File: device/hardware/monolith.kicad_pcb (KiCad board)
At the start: 2 copper layers, 116 parts, among them J1 CAN, J10 Conn_01x02_Pin, J11 UART, J12 DIN1/2, J13 DIN3/4, J14 Micro_SD_Card, J2 GPS, J3 I2C, J4 AIN1/2, J5 AIN3/4, J6 AIN5/6, J7 Conn_01x02_Pin, J8 Conn_01x02_Pin, J9 Conn_01x02_Pin, U1 ESP32-S3-WROOM-1-N4, U10 LMV321, U11 AMS1117-3.3, U2 MCP6002-xSN, U3 SN65HVD230, U4 TPS5430DDA, U5 MCP6002-xSN, U6 MPU-6050, U7 MCP6002-xSN, U8 AMS1117-3.3, U9 PCF8563T, Y1 FC135

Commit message: update: PCB prototype
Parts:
- removed C19: 47uF, Capacitor_SMD:C_1206_3216Metric
- removed RV1, RV2, RV3, RV4: 1k, Potentiometer_THT:Potentiometer_Bourns_3266W_Vertical
- removed TP3, TP4, TP5, TP6: TestPoint, Connector_PinHeader_2.54mm:PinHeader_1x01_P2.54mm_Vertical
- added C29: 0.1uF, Capacitor_SMD:C_0603_1608Metric, F.Cu at (97.9, 118.6)
- added C30: 22uF, Capacitor_SMD:C_0603_1608Metric, F.Cu at (147.8, 112.6)
- added C31: 22nF, Capacitor_SMD:C_0603_1608Metric, F.Cu at (125.5, 116.7)
- added C32: 22nF, Capacitor_SMD:C_0603_1608Metric, F.Cu at (128.9, 116.7)
- added C33: 22nF, Capacitor_SMD:C_0603_1608Metric, F.Cu at (136.6, 116.7)
- added C34: 22nF, Capacitor_SMD:C_0603_1608Metric, F.Cu at (140.0, 116.7)
- added C35: 22nF, Capacitor_SMD:C_0603_1608Metric, F.Cu at (147.8, 119.9)
- added C36: 22nF, Capacitor_SMD:C_0603_1608Metric, F.Cu at (151.0, 119.9)
- added C37: 22nF, Capacitor_SMD:C_0603_1608Metric, F.Cu at (155.5, 119.2)
- added C38: 0.1uF, Capacitor_SMD:C_0603_1608Metric, F.Cu at (70.4, 114.9)
- added JP6: Jumper_2_Small_Open, Connector_PinHeader_2.54mm:PinHeader_1x02_P2.54mm_Vertical, F.Cu at (136.2, 134.4)
- added JP7: Jumper_2_Small_Open, Connector_PinHeader_2.54mm:PinHeader_1x02_P2.54mm_Vertical, F.Cu at (140.4, 134.4)
- added JP8: TERMINAL, Connector_PinHeader_2.54mm:PinHeader_1x02_P2.54mm_Vertical, F.Cu at (72.2, 130.1)
- added JP9: Jumper_2_Small_Bridged, Jumper:SolderJumper-2_P1.3mm_Bridged_RoundedPad1.0x1.5mm, F.Cu at (147.7, 107.1)
- added R32: 220, Resistor_SMD:R_0603_1608Metric, F.Cu at (114.0, 138.4)
- added R33: 4.7k, Resistor_SMD:R_0603_1608Metric, F.Cu at (106.3, 116.6)
- added R34: 100, Resistor_SMD:R_0603_1608Metric, F.Cu at (157.9, 120.0)
- added R35: 220, Resistor_SMD:R_0603_1608Metric, F.Cu at (107.1, 138.4)
- added R36: 220, Resistor_SMD:R_0603_1608Metric, F.Cu at (102.9, 138.4)
- added R37: 4.7k, Resistor_SMD:R_0603_1608Metric, F.Cu at (108.0, 115.8)
- added R38: 4.7k, Resistor_SMD:R_0603_1608Metric, F.Cu at (118.2, 115.0)
- added R39: 4.7k, Resistor_SMD:R_0603_1608Metric, F.Cu at (119.9, 115.8)
- added REF**: MountingHole_3mm_Pad_TopBottom, MountingHole:MountingHole_3mm_Pad_TopBottom, F.Cu at (68.3, 88.2)
- added REF**: MountingHole_3mm_Pad_TopBottom, MountingHole:MountingHole_3mm_Pad_TopBottom, F.Cu at (156.3, 136.8)
- added REF**: MountingHole_3mm_Pad_TopBottom, MountingHole:MountingHole_3mm_Pad_TopBottom, F.Cu at (68.3, 136.8)
- added REF**: MountingHole_3mm_Pad_TopBottom, MountingHole:MountingHole_3mm_Pad_TopBottom, F.Cu at (138.8, 88.2)
- added U12: AMS1117-3.3, Package_TO_SOT_SMD:SOT-223-3_TabPin2, F.Cu at (142.4, 109.6)
- added U13: ADS1115IDGS, Package_SO:TSSOP-10_3x3mm_P0.5mm, F.Cu at (150.4, 115.8)
- C13, C14: value 47uF -> 22nF; footprint Capacitor_SMD:C_1206_3216Metric -> Capacitor_SMD:C_0603_1608Metric
- C16: value 0.1uF -> 47uF; footprint Capacitor_SMD:C_0603_1608Metric -> Capacitor_SMD:C_1206_3216Metric
- C17: value 22nF -> 47uF; footprint Capacitor_SMD:C_0603_1608Metric -> Capacitor_SMD:C_1206_3216Metric
- C18: value 22nF -> 0.1uF
- C22, C28: value 22uF -> 0.1uF
- C23: value 20pF -> 22uF
- C25: value 22nF -> 20pF
- C26: value 10uF -> 22nF
- C27: value 0.1uF -> 10uF
- J1, J2, J3, J4, J5, J6: footprint Connector_Molex:Molex_Mini-Fit_Jr_5566-04A2_2x02_P4.20mm_Vertical -> Connector_Molex:Molex_Mini-Fit_Jr_5569-04A2_2x02_P4.20mm_Horizontal
- J10: value Conn_01x02_Pin -> UART; footprint Connector_PinHeader_2.54mm:PinHeader_1x02_P2.54mm_Vertical -> Connector_PinHeader_2.54mm:PinHeader_1x04_P2.54mm_Vertical
- J11: value UART -> DIN1/2; footprint Connector_PinHeader_2.54mm:PinHeader_1x04_P2.54mm_Vertical -> Connector_Molex:Molex_Mini-Fit_Jr_5569-04A2_2x02_P4.20mm_Horizontal
- J12: value DIN1/2 -> DIN3/4; footprint Connector_Molex:Molex_Mini-Fit_Jr_5566-04A2_2x02_P4.20mm_Vertical -> Connector_Molex:Molex_Mini-Fit_Jr_5569-04A2_2x02_P4.20mm_Horizontal
- J13: value DIN3/4 -> Micro_SD_Card; footprint Connector_Molex:Molex_Mini-Fit_Jr_5566-04A2_2x02_P4.20mm_Vertical -> parts:TF115BCP9
- J14: value Micro_SD_Card -> I2C2; footprint parts:TF115BCP9 -> Connector_PinHeader_1.00mm:PinHeader_1x02_P1.00mm_Vertical
- J7: value Conn_01x02_Pin -> USB; footprint Connector_PinHeader_2.54mm:PinHeader_1x02_P2.54mm_Vertical -> Connector_PinHeader_1.00mm:PinHeader_1x02_P1.00mm_Vertical
- J8: value Conn_01x02_Pin -> CAN; footprint Connector_PinHeader_2.54mm:PinHeader_1x02_P2.54mm_Vertical -> Connector_PinHeader_1.00mm:PinHeader_1x02_P1.00mm_Vertical
- J9: value Conn_01x02_Pin -> I2C1; footprint Connector_PinHeader_2.54mm:PinHeader_1x02_P2.54mm_Vertical -> Connector_PinHeader_1.00mm:PinHeader_1x02_P1.00mm_Vertical
- JP1: value Jumper_2_Small_Open -> RESET; footprint Connector_PinHeader_2.54mm:PinHeader_1x02_P2.54mm_Vertical -> Connector_PinHeader_1.00mm:PinHeader_1x02_P1.00mm_Vertical
- JP4: value Jumper_2_Small_Open -> BOOT; footprint Connector_PinHeader_2.54mm:PinHeader_1x02_P2.54mm_Vertical -> Connector_PinHeader_1.00mm:PinHeader_1x02_P1.00mm_Vertical
- JP5: value Jumper_2_Small_Bridged -> BTN; footprint Jumper:SolderJumper-2_P1.3mm_Bridged_RoundedPad1.0x1.5mm -> Connector_PinHeader_1.00mm:PinHeader_1x02_P1.00mm_Vertical
- R10, R11, R12, R3, R9: value 10k -> 1k
- R13: value 120 -> 10k
- R14, R15, R24, R5: value 100 -> 10k
- R16, R17: value 10k -> 100
- R19: value 10k -> 120
- R20: value 3.3k -> 10k
- R21: value 1k -> 10k
- R23, R4: value 100 -> 1k
- R25: value 15k -> 10k
- R26: value 430 -> 3.3k
- R27, R28: value 220 -> 100
- R29: value 220 -> 15k
- R30: value 220 -> 430
- R31: value 100 -> 220
- R6, R7: value 1k -> 100
- TP1, TP2: footprint Connector_PinHeader_2.54mm:PinHeader_1x01_P2.54mm_Vertical -> Connector_PinHeader_1.00mm:PinHeader_1x01_P1.00mm_Vertical
- U1: value ESP32-S3-WROOM-1-N4 -> MCP6002-xSN; footprint RF_Module:ESP32-S3-WROOM-1 -> Package_SO:SOIC-8_3.9x4.9mm_P1.27mm
- U11: value AMS1117-3.3 -> PCF8563T; footprint Package_TO_SOT_SMD:SOT-223-3_TabPin2 -> Package_SO:SOIC-8_3.9x4.9mm_P1.27mm
- U2: value MCP6002-xSN -> ESP32-S3-WROOM-1-N4; footprint Package_SO:SOIC-8_3.9x4.9mm_P1.27mm -> RF_Module:ESP32-S3-WROOM-1
- U3: value SN65HVD230 -> MCP6002-xSN
- U4: value TPS5430DDA -> SN65HVD230; footprint Package_SO:TI_SO-PowerPAD-8_ThermalVias -> Package_SO:SOIC-8_3.9x4.9mm_P1.27mm
- U5: value MCP6002-xSN -> TPS5430DDA; footprint Package_SO:SOIC-8_3.9x4.9mm_P1.27mm -> Package_SO:TI_SO-PowerPAD-8_ThermalVias
- U6: value MPU-6050 -> MCP6002-xSN; footprint Sensor_Motion:InvenSense_QFN-24_4x4mm_P0.5mm -> Package_SO:SOIC-8_3.9x4.9mm_P1.27mm
- U7: value MCP6002-xSN -> MPU-6050; footprint Package_SO:SOIC-8_3.9x4.9mm_P1.27mm -> Sensor_Motion:InvenSense_QFN-24_4x4mm_P0.5mm
- U9: value PCF8563T -> ADS1115IDGS; footprint Package_SO:SOIC-8_3.9x4.9mm_P1.27mm -> Package_SO:TSSOP-10_3x3mm_P0.5mm
- moved J1 110.9 mm to (73.8, 148.3), turned to 180 degrees
- moved U4 95.9 mm to (70.2, 119.4), turned to -90 degrees
- moved J2 93.0 mm to (96.0, 148.3), turned to 180 degrees
- moved U1 88.4 mm to (127.2, 123.6)
- moved J3 82.6 mm to (84.9, 148.3), turned to 180 degrees
- moved R13 82.2 mm to (72.2, 124.8), turned to 90 degrees
- moved U8 80.3 mm to (97.8, 135.5), turned to 90 degrees
- moved L1 79.0 mm to (89.0, 135.5), turned to 90 degrees
- moved R19 78.8 mm to (73.0, 132.7)
- moved R26 73.2 mm to (82.7, 124.5)
- moved R25 72.5 mm to (83.5, 122.0), turned to 90 degrees
- moved J4 69.0 mm to (129.3, 148.3), turned to 180 degrees
- moved D12 68.2 mm to (98.8, 114.3)
- moved U11 67.2 mm to (101.6, 120.3), turned to 90 degrees
- moved J11 61.6 mm to (118.2, 148.3), turned to 180 degrees
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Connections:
- C10 pad 1: Net-(U6-CPOUT) -> Net-(U7-CPOUT)
- C11 pad 1: Net-(U6-REGOUT) -> Net-(U7-REGOUT)
- C13 pad 1: +5V -> GNDA
- C13 pad 2: GND -> Net-(D7-A1)
- C14 pad 1: +5V -> GNDA
- C14 pad 2: GND -> Net-(D8-A1)
- C16 pad 1: +3V3 -> +5V
- C17 pad 1: GNDA -> +5V
- C17 pad 2: Net-(D7-A1) -> GND
- C18 pad 1: GNDA -> +3V3
- C18 pad 2: Net-(D8-A1) -> GND
- C22 pad 1: GND -> +3.3VA
- C22 pad 2: +3V3 -> GNDA
- C23 pad 2: Net-(U9-OSCI) -> +3V3
- C24 pad 2: Net-(U9-OSCO) -> Net-(U11-OSCI)
- C25 pad 1: GNDA -> GND
- C25 pad 2: Net-(D9-A1) -> Net-(U11-OSCO)
- C26 pad 1: GND -> GNDA
- C26 pad 2: +5V -> Net-(D9-A1)
- C27 pad 1: Net-(U9-VDD) -> GND
- C27 pad 2: GND -> +5V
- C28 pad 1: GNDA -> +3.3VA
- C28 pad 2: +3.3VA -> GNDA
- C9 pad 1: Net-(U4-BOOT) -> Net-(U5-BOOT)
- D12 pad 3: Net-(U9-VDD) -> Net-(U11-VDD)
- J10 pad 1: /SDA -> +3V3
- J10 pad 2: /SCL -> Net-(J10-Pin_2)
- J11 pad 1: +3V3 -> GND
- J11 pad 2: Net-(J11-Pin_2) -> +5V
- J11 pad 3: Net-(J11-Pin_3) -> /DIN1
- J11 pad 4: GND -> /DIN2
- J12 pad 1: +5V -> GND
- J12 pad 2: GND -> +5V
- J12 pad 3: /DIN1 -> /DIN3
- J12 pad 4: /DIN2 -> /DIN4
- J13 pad 1: +5V -> /DAT2
- J13 pad 2: GND -> /DAT3
- J13 pad 3: /DIN3 -> /CMD
- J13 pad 4: /DIN4 -> +3V3
- J14 pad 1: /DAT2 -> /SDA2
- J14 pad 2: /DAT3 -> /SCL2
- J2 pad 1: +5V -> +3V3
- J3 pad 1: +5V -> +3V3
- J3 pad 3: /I2C_SCL -> /RX
- J3 pad 4: /I2C_SDA -> /TX
- J4 pad 1: +5V -> GNDA
- J4 pad 2: GND -> +5V
- J4 pad 3: /AIN1 -> /AIN2
- J4 pad 4: /AIN2 -> /AIN1
- J5 pad 1: +5V -> GNDA
- J5 pad 2: GND -> +5V
- J5 pad 3: /AIN3 -> /AIN4
- J5 pad 4: /AIN4 -> /AIN3
- J6 pad 1: +5V -> GNDA
- J6 pad 2: GND -> +5V
- J6 pad 3: /AIN5 -> /AIN6
- J6 pad 4: /AIN6 -> /AIN5
- J7 pad 1: /GPS_RX -> Net-(J7-Pin_1)
- J7 pad 2: /GPS_TX -> Net-(J7-Pin_2)
- J8 pad 1: Net-(J8-Pin_1) -> /CANRX
- J8 pad 2: Net-(J8-Pin_2) -> /CANTX
- J9 pad 1: /CANTX -> /SDA1
- J9 pad 2: /CANRX -> /SCL1
- JP2 pad 1: GND -> Net-(D1-A1)
- JP3 pad 1: +3V3 -> Net-(D2-A1)
- JP4 pad 1: Net-(JP4-A) -> GND
- JP4 pad 2: /CANL -> Net-(JP4-B)
- JP5 pad 1: GND -> +3V3
- JP5 pad 2: GNDA -> Net-(JP5-B)
- R10 pad 1: /DAT1 -> /AIN4
- R10 pad 2: +3V3 -> Net-(D5-A1)
- R11 pad 1: /DAT0 -> GNDA
- R11 pad 2: +3V3 -> Net-(JP6-B)
- R12 pad 1: /CLK -> GNDA
- R12 pad 2: +3V3 -> Net-(JP7-B)
- R13 pad 1: Net-(JP4-A) -> GND
- R13 pad 2: /CANH -> Net-(U4-Rs)
- R14 pad 1: Net-(U5A--) -> /DAT1
- R14 pad 2: /ADC3 -> +3V3
- R15 pad 1: Net-(U5B--) -> /DAT0
- R15 pad 2: /ADC4 -> +3V3
- R16 pad 1: /CMD -> Net-(U3A--)
- R16 pad 2: +3V3 -> /ADC3
- R17 pad 1: /DAT3 -> Net-(U3B--)
- R17 pad 2: +3V3 -> /ADC4
- R18 pad 1: /DAT2 -> /CLK
- R19 pad 1: Net-(U4-VSENSE) -> Net-(JP8-A)
- R19 pad 2: +5V -> /CANH
- R20 pad 1: GND -> /CMD
- R20 pad 2: Net-(U4-VSENSE) -> +3V3
- R21 pad 1: /AIN5 -> /DAT3
- R21 pad 2: Net-(D7-A1) -> +3V3
- R22 pad 1: /AIN6 -> /AIN5
- R22 pad 2: Net-(D8-A1) -> Net-(D7-A1)
- R23 pad 1: Net-(U7A--) -> /AIN6
- R23 pad 2: /ADC5 -> Net-(D8-A1)
- R24 pad 1: Net-(U7B--) -> /DAT2
- R24 pad 2: /ADC6 -> +3V3
- R25 pad 1: Net-(D9-A1) -> Net-(U5-VSENSE)
- R25 pad 2: VBUS -> +5V
- R26 pad 1: GNDA -> GND
- R26 pad 2: Net-(D9-A1) -> Net-(U5-VSENSE)
- R27 pad 1: /DIN1 -> Net-(U6A--)
- R27 pad 2: /D1 -> /ADC5
- R28 pad 1: /DIN2 -> Net-(U6B--)
- R28 pad 2: /D2 -> /ADC6
- R29 pad 1: /DIN3 -> Net-(D9-A1)
- R29 pad 2: /D3 -> VBUS
- R3 pad 1: Net-(JP1-B) -> GNDA
- R3 pad 2: +3V3 -> Net-(JP2-B)
- R30 pad 1: /DIN4 -> GNDA
- R30 pad 2: /D4 -> Net-(D9-A1)
- R31 pad 1: Net-(U10--) -> /DIN1
- R31 pad 2: /ADC7 -> /D1
- R4 pad 1: Net-(U2A--) -> GNDA
- R4 pad 2: /ADC1 -> Net-(JP3-B)
- R5 pad 1: Net-(U2B--) -> Net-(JP1-B)
- R5 pad 2: /ADC2 -> +3V3
- R6 pad 1: Net-(D3-K) -> Net-(U1A--)
- R6 pad 2: +3V3 -> /ADC1
- R7 pad 1: /AIN3 -> Net-(U1B--)
- R7 pad 2: Net-(D4-A1) -> /ADC2
- R8 pad 1: /AIN4 -> +3V3
- R8 pad 2: Net-(D5-A1) -> Net-(D3-K)
- R9 pad 1: GND -> /AIN3
- R9 pad 2: Net-(U3-Rs) -> Net-(D4-A1)
- TP1 pad 1: Net-(D1-A1) -> Net-(D7-A1)
- TP2 pad 1: Net-(D2-A1) -> Net-(D8-A1)
- U1 pad 1: GND -> Net-(U1A--)
- U1 pad 2: +3V3 -> Net-(U1A--)
- U1 pad 3: Net-(JP1-B) -> Net-(D1-A1)
- U1 pad 4: /ADC1 -> GNDA
- U1 pad 5: /ADC2 -> Net-(D2-A1)
- U1 pad 6: /ADC3 -> Net-(U1B--)
- U1 pad 7: /ADC4 -> Net-(U1B--)
- U1 pad 8: /I2C_SCL -> +3.3VA
- U11 pad 1: GND -> Net-(U11-OSCI)
- U11 pad 2: +3.3VA -> Net-(U11-OSCO)
- U11 pad 3: +5V -> unconnected-(U11-~{INT}-Pad3)
- U2 pad 1: Net-(U2A--) -> GND
- U2 pad 2: Net-(U2A--) -> +3V3
- U2 pad 3: Net-(D1-A1) -> Net-(JP1-B)
- U2 pad 4: GNDA -> unconnected-(U2-IO4-Pad4)
- U2 pad 5: Net-(D2-A1) -> Net-(D3-A)
- U2 pad 6: Net-(U2B--) -> /CANRX
- U2 pad 7: Net-(U2B--) -> /CANTX
- U2 pad 8: +3.3VA -> /TX
- U3 pad 1: /CANTX -> Net-(U3A--)
- U3 pad 2: GND -> Net-(U3A--)
- U3 pad 3: +3V3 -> Net-(D4-A1)
- U3 pad 4: /CANRX -> GNDA
- U3 pad 5: unconnected-(U3-Vref-Pad5) -> Net-(D5-A1)
- U3 pad 6: /CANL -> Net-(U3B--)
- U3 pad 7: /CANH -> Net-(U3B--)
- U3 pad 8: Net-(U3-Rs) -> +3.3VA
- U4 pad 1: Net-(U4-BOOT) -> /CANTX
- U4 pad 2: unconnected-(U4-NC-Pad2) -> GND
- U4 pad 3: unconnected-(U4-NC-Pad3) -> +3V3
- U4 pad 4: Net-(U4-VSENSE) -> /CANRX
- U4 pad 6: GND -> /CANL
- U4 pad 7: VBUS -> /CANH
- U4 pad 8: Net-(D6-K) -> Net-(U4-Rs)
- U5 pad 1: Net-(U5A--) -> Net-(U5-BOOT)
- U5 pad 2: Net-(U5A--) -> unconnected-(U5-NC-Pad2)
- U5 pad 3: Net-(D4-A1) -> unconnected-(U5-NC-Pad3)
- U5 pad 4: GNDA -> Net-(U5-VSENSE)
- U5 pad 5: Net-(D5-A1) -> unconnected-(U5-EN-Pad5)
- U5 pad 6: Net-(U5B--) -> GND
- U5 pad 7: Net-(U5B--) -> VBUS
- U5 pad 8: +3.3VA -> Net-(D6-K)
- U6 pad 1: GND -> Net-(U6A--)
- U6 pad 2: unconnected-(U6-NC-Pad2) -> Net-(U6A--)
- U6 pad 3: unconnected-(U6-NC-Pad3) -> Net-(D7-A1)
- U6 pad 4: unconnected-(U6-NC-Pad4) -> GNDA
- U6 pad 5: unconnected-(U6-NC-Pad5) -> Net-(D8-A1)
- U6 pad 6: unconnected-(U6-AUX_DA-Pad6) -> Net-(U6B--)
- U6 pad 7: unconnected-(U6-AUX_CL-Pad7) -> Net-(U6B--)
- U6 pad 8: +3V3 -> +3.3VA
- U7 pad 1: Net-(U7A--) -> GND
- U7 pad 2: Net-(U7A--) -> unconnected-(U7-NC-Pad2)
- U7 pad 3: Net-(D7-A1) -> unconnected-(U7-NC-Pad3)
- U7 pad 4: GNDA -> unconnected-(U7-NC-Pad4)
- U7 pad 5: Net-(D8-A1) -> unconnected-(U7-NC-Pad5)
- U7 pad 6: Net-(U7B--) -> unconnected-(U7-AUX_DA-Pad6)
- U7 pad 7: Net-(U7B--) -> unconnected-(U7-AUX_CL-Pad7)
- U7 pad 8: +3.3VA -> +3V3
- U9 pad 1: Net-(U9-OSCI) -> GNDA
- U9 pad 2: Net-(U9-OSCO) -> unconnected-(U9-ALERT/RDY-Pad2)
- U9 pad 3: unconnected-(U9-~{INT}-Pad3) -> GNDA
- U9 pad 4: GND -> /ADC1
- U9 pad 5: /SDA -> /ADC2
- U9 pad 6: /SCL -> /ADC3
- U9 pad 7: unconnected-(U9-CLKO-Pad7) -> /ADC4
- U9 pad 8: Net-(U9-VDD) -> +3.3VA
- Y1 pad 1: Net-(U9-OSCI) -> Net-(U11-OSCI)
- Y1 pad 2: Net-(U9-OSCO) -> Net-(U11-OSCO)
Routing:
- net +3V3: track 0.00 -> 230.9 mm, vias 0 -> 6
- net +5V: track 0.00 -> 164.4 mm, vias 0 -> 2
- net VBUS: track 0.00 -> 123.3 mm, vias 0 -> 2
- net +3.3VA: track 0.00 -> 60.2 mm
- net /TX: track 0.00 -> 52.5 mm, vias 0 -> 1
- net /RX: track 0.00 -> 49.5 mm, vias 0 -> 1
- net /SDA1: track 0.00 -> 46.7 mm
- net /GPS_TX: track 0.00 -> 45.4 mm, vias 0 -> 1
- net /SCL1: track 0.00 -> 45.1 mm
- net /GPS_RX: track 0.00 -> 44.8 mm, vias 0 -> 1
- net /CANRX: track 0.00 -> 42.1 mm
- net /CANTX: track 0.00 -> 37.9 mm
- net /D1: track 0.00 -> 30.0 mm, vias 0 -> 2
- net /D2: track 0.00 -> 28.8 mm, vias 0 -> 2
- net /D4: track 0.00 -> 27.9 mm, vias 0 -> 2
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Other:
- board outline added: 96 x 74.4 mm

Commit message: update: prototype PCB
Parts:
- added C19: 0.1uF, Capacitor_SMD:C_0603_1608Metric, F.Cu at (101.3, 96.6)
- added C39: 0.1uF, Capacitor_SMD:C_0603_1608Metric, F.Cu at (123.1, 109.0)
- added G***: LOGO, LOGO, F.Cu at (74.2, 88.3)
- added G***: LOGO, parts:luftaquila, F.Cu at (125.8, 95.7)
- added Q1: SS8050, Package_TO_SOT_SMD:SOT-23, F.Cu at (89.2, 97.6)
- added Q2: SS8050, Package_TO_SOT_SMD:SOT-23, F.Cu at (89.2, 94.1)
- added R40: 10k, Resistor_SMD:R_0603_1608Metric, F.Cu at (85.5, 93.2)
- added R41: 10k, Resistor_SMD:R_0603_1608Metric, F.Cu at (85.5, 96.7)
- C1: value 1uF -> 10uF
- C5: value 10uF -> 1uF
- D1, D2, D4, D5, D7, D8, D9: value H5VL06B -> H5VLD3B; footprint Diode_SMD:D_0603_1608Metric -> Diode_SMD:D_SOD-323
- J10: footprint Connector_PinHeader_2.54mm:PinHeader_1x04_P2.54mm_Vertical -> Connector_PinHeader_2.54mm:PinHeader_2x03_P2.54mm_Vertical
- JP1: value RESET -> EN
- JP5: value BTN -> RST
- JP8: value TERMINAL -> CAN 120Ω
- moved J10 55.7 mm to (70.0, 99.9), turned to 180 degrees
- moved JP4 31.0 mm to (93.7, 97.6), turned to -90 degrees
- moved REF** 26.7 mm to (156.3, 108.3)
- moved JP5 23.0 mm to (116.2, 115.8), turned to 90 degrees
- moved C21 12.1 mm to (103.2, 138.8), turned to 180 degrees
- moved D14 5.70 mm to (108.6, 134.1)
- moved R36 5.70 mm to (108.6, 138.4)
- moved R37 4.99 mm to (103.6, 113.6), turned to 0 degrees
- moved C23 4.27 mm to (100.8, 128.3), turned to 180 degrees
- moved R24 4.11 mm to (139.7, 92.1)
- moved D13 3.95 mm to (111.0, 134.1)
- moved R35 3.95 mm to (111.0, 138.4)
- moved J14 3.35 mm to (108.0, 113.2)
- moved JP1 3.32 mm to (93.7, 95.2), turned to -90 degrees
- moved C5 3.21 mm to (99.8, 96.6)
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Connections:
- C1 pad 1: GND -> +3V3
- C1 pad 2: Net-(JP1-B) -> GND
- C4 pad 1: GND -> +3V3
- C4 pad 2: +3V3 -> GND
- C5 pad 1: GND -> /EN
- C5 pad 2: +3V3 -> GND
- D10 pad 1: /D1 -> /D4
- D11 pad 1: /D2 -> /D3
- D13 pad 1: /D3 -> /D2
- D14 pad 1: /D4 -> /D1
- J10 pad 2: Net-(J10-Pin_2) -> GND
- J10 pad 3: Net-(J10-Pin_3) -> /RX
- J10 pad 4: GND -> /RTS
- J11 pad 1: GND -> +5V
- J11 pad 2: +5V -> GND
- J11 pad 3: /DIN1 -> /DIN4
- J11 pad 4: /DIN2 -> /DIN3
- J12 pad 1: GND -> +5V
- J12 pad 2: +5V -> GND
- J12 pad 3: /DIN3 -> /DIN2
- J12 pad 4: /DIN4 -> /DIN1
- J3 pad 3: /RX -> /DBGRX
- J3 pad 4: /TX -> /DBGTX
- J4 pad 1: GNDA -> +5V
- J4 pad 2: +5V -> GNDA
- J5 pad 1: GNDA -> +5V
- J5 pad 2: +5V -> GNDA
- J6 pad 1: GNDA -> +5V
- J6 pad 2: +5V -> GNDA
- JP1 pad 1: GND -> /EN
- JP1 pad 2: Net-(JP1-B) -> GND
- JP4 pad 1: GND -> /BOOT
- JP4 pad 2: Net-(JP4-B) -> GND
- JP5 pad 1: +3V3 -> Net-(JP5-A)
- JP5 pad 2: Net-(JP5-B) -> +3V3
- R31 pad 1: /DIN1 -> /DIN4
- R31 pad 2: /D1 -> /D4
- R32 pad 1: /DIN2 -> /DIN3
- R32 pad 2: /D2 -> /D3
- R33 pad 1: +3V3 -> /SDA2
- R33 pad 2: /SDA2 -> +3V3
- R35 pad 1: /DIN3 -> /DIN2
- R35 pad 2: /D3 -> /D2
- R36 pad 1: /DIN4 -> /DIN1
- R36 pad 2: /D4 -> /D1
- R37 pad 1: /SCL2 -> +3V3
- R37 pad 2: +3V3 -> /SCL2
- R38 pad 1: /SCL1 -> +3V3
- R38 pad 2: +3V3 -> /SCL1
- R39 pad 1: +3V3 -> /SDA1
- R39 pad 2: /SDA1 -> +3V3
- R5 pad 1: Net-(JP1-B) -> /EN
- U2 pad 10: Net-(J7-Pin_1) -> /GPS_TX
- U2 pad 11: Net-(J7-Pin_2) -> /GPS_RX
- U2 pad 13: /GPS_TX -> Net-(J7-Pin_1)
- U2 pad 14: /GPS_RX -> Net-(J7-Pin_2)
- U2 pad 17: /D4 -> /SDA2
- U2 pad 18: /D3 -> /SCL2
- U2 pad 19: /D2 -> /D1
- U2 pad 20: /D1 -> /D2
- U2 pad 21: /SDA2 -> /D3
- U2 pad 22: /SCL2 -> /D4
- U2 pad 23: unconnected-(U2-IO21-Pad23) -> Net-(JP5-A)
- U2 pad 27: Net-(JP4-B) -> /BOOT
- U2 pad 3: Net-(JP1-B) -> /EN
- U2 pad 36: Net-(J10-Pin_3) -> /RX
- U2 pad 37: Net-(J10-Pin_2) -> /TX
- U2 pad 38: Net-(JP5-B) -> unconnected-(U2-IO2-Pad38)
- U2 pad 8: /TX -> /DBGTX
- U2 pad 9: /RX -> /DBGRX
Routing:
- net GND: track 0.00 -> 100.3 mm, vias 0 -> 73
- net GNDA: track 2.49 -> 66.1 mm, vias 0 -> 28
- net /DBGTX: track 0.00 -> 54.6 mm, vias 0 -> 1
- net /DBGRX: track 0.00 -> 51.3 mm, vias 0 -> 1
- net /BOOT: track 0.00 -> 39.3 mm, vias 0 -> 1
- net /DTR: track 0.00 -> 25.8 mm, vias 0 -> 2
- net /RTS: track 0.00 -> 22.2 mm
- net /EN: track 0.00 -> 15.8 mm, vias 0 -> 1
- net Net-(J10-Pin_3): track 13.8 -> 0.00 mm
- net +3V3: track 230.9 -> 242.5 mm, vias 6 -> 8
- net Net-(J10-Pin_2): track 10.7 -> 0.00 mm
- net +5V: track 164.4 -> 170.8 mm
- net Net-(JP1-B): track 6.19 -> 0.00 mm
- net Net-(JP5-A): track 0.00 -> 5.04 mm
- net /RX: track 49.5 -> 54.3 mm
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- added copper zone on B.Cu, net GND
- added copper zone on F.Cu, net GND
- added copper zone on B.Cu, net GNDA
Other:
- board text added: "+X"
- board text added: "+Y"
- board text added: "+Z"
- board text added: "2.0.0"
- board text added: "3V3"
- board text added: "5V"
- board text added: "AIN"
- board text added: "AIN1"
- board text added: "AIN2"
- board text added: "AIN3"
- board text added: "AIN4"
- board text added: "AIN5"
- board text added: "AIN6"
- board text added: "CANH"
- board text added: "CANL"
- board text added: "D+"
- board text added: "D-"
- board text added: "DBGRX"
- board text added: "DBGTX"
- board text added: "DEBUG"
- board text added: "DIN"
- board text added: "DIN1"
- board text added: "DIN2"
- board text added: "DIN3"
- board text added: "DIN4"
- board text added: "DTR"
- board text added: "Every car is a human-guided missile if you operate it wrong enough"
- board text added: "GND"
- board text added: "GPS"
- board text added: "GPSRX"
- board text added: "GPSTX"
- board text added: "JLCJLCJLCJLC"
- board text added: "JLCPCB QR PLACEHOLDER"
- board text added: "PWR/CAN"
- board text added: "RTS"
- board text added: "RX"
- board text added: "SCL"
- board text added: "SDA"
- board text added: "TX"
- board text added: "VIN"
- board text added: "h"
- board text added: "https://github.com/luftaquila/monolith"
- board text added: "i"
- board text added: "l"
- board text added: "m"
- board text added: "n"
- board text added: "o"
- board text added: "t"
- board text added: "v"
- board text added: "{dblquote}THE BEERWARE LICENSE{dblquote} (Revision 42): LUFT-AQUILA wrote this project. As long as you retain this notice, you can do whatever you want with this stuff. If we meet someday, and you think this stuff is worth it, you can buy me a beer in return."
- board text added: "↑"
- board text added: "→"

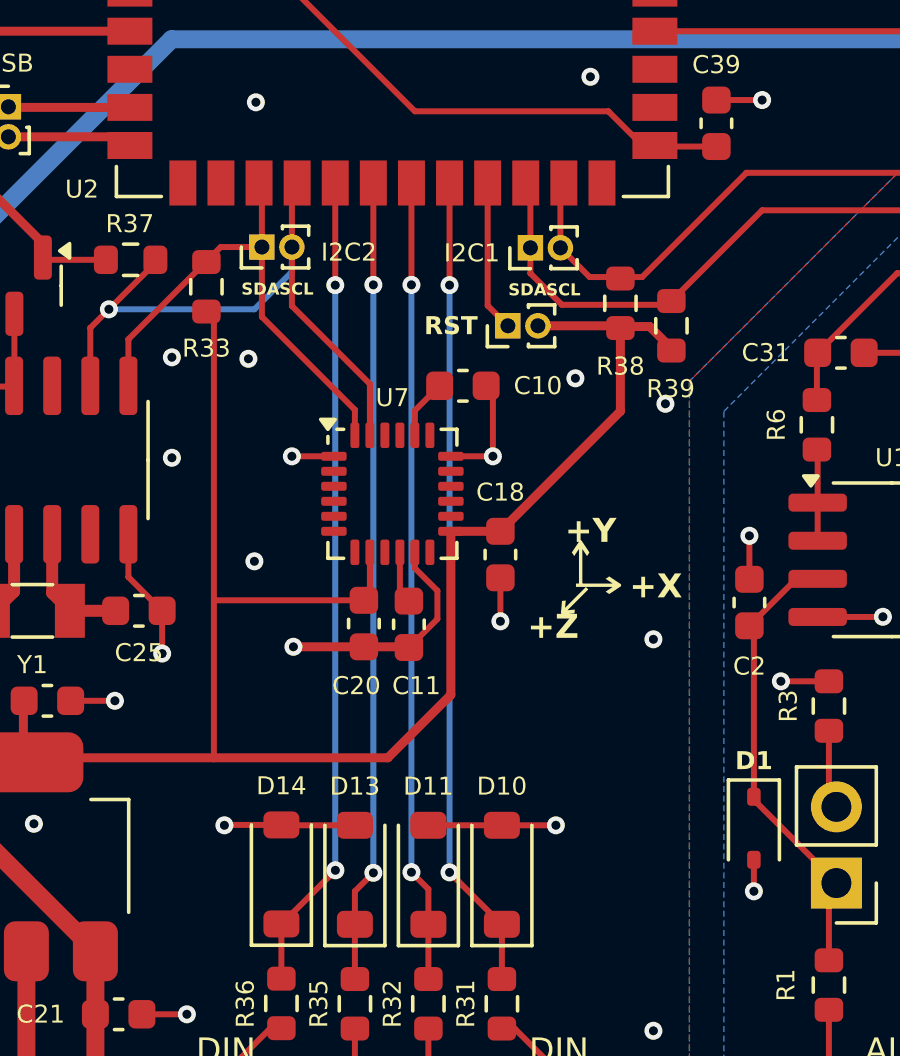
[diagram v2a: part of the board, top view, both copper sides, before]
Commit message: update: replace MPU-6050 to MPU-6500
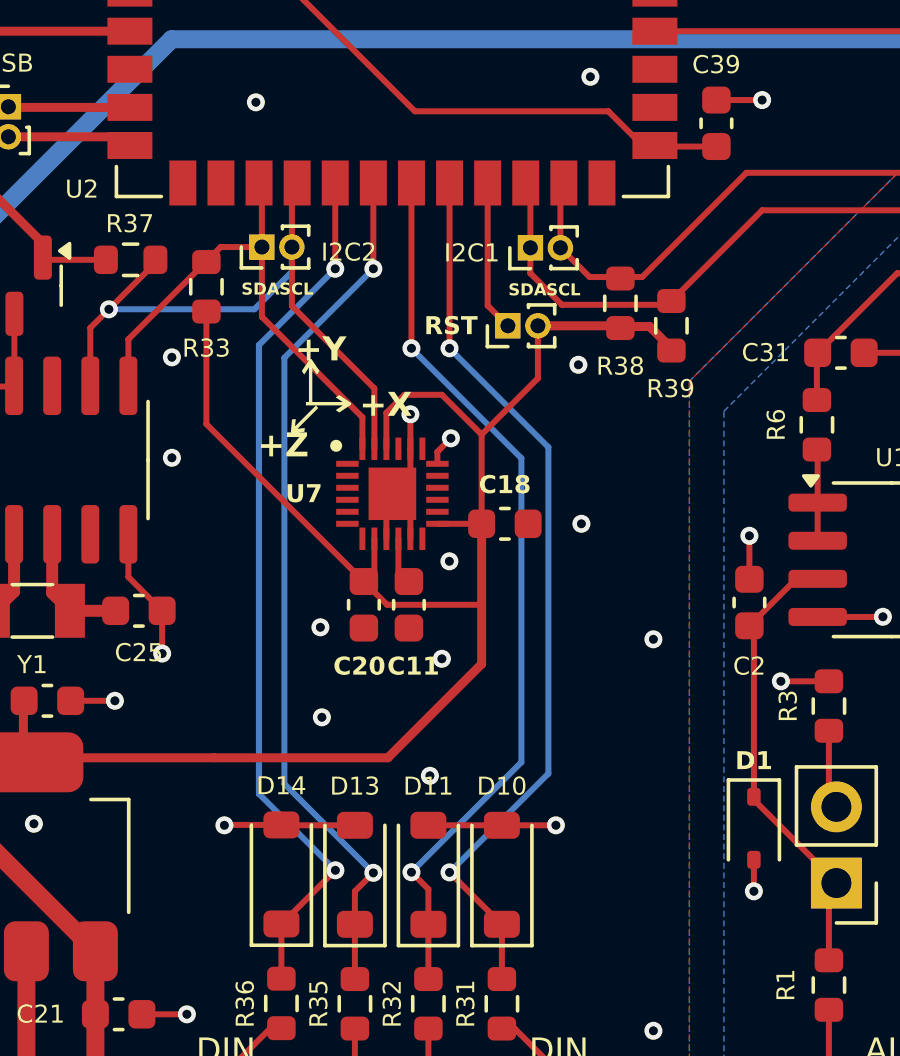
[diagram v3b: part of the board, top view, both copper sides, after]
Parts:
- removed C10: 2.2nF, Capacitor_SMD:C_0603_1608Metric
- U7: value MPU-6050 -> MPU-6500; footprint Sensor_Motion:InvenSense_QFN-24_4x4mm_P0.5mm -> parts:QFN40P300X300X95-25N-D
- moved C18 1.04 mm to (116.0, 122.4), turned to 0 degrees
- moved C11 0.65 mm to (112.8, 125.1), turned to 90 degrees
- moved C20 0.62 mm to (111.3, 125.1), turned to -90 degrees
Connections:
- C11 pad 1: Net-(U7-REGOUT) -> GND
- C11 pad 2: GND -> Net-(U7-REGOUT)
- C20 pad 1: GND -> +3V3
- C20 pad 2: +3V3 -> GND
- U7 pad 1: GND -> unconnected-(U7-NC_1-Pad1)
- U7 pad 20: Net-(U7-CPOUT) -> GND
- U7 pad 22: unconnected-(U7-RESV-Pad22) -> +3V3
- U7 pad 9: unconnected-(U7-AD0-Pad9) -> GND
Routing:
- net GND: track 100.3 -> 93.1 mm, vias 73 -> 74
- net /D3: track 26.8 -> 29.8 mm
- net /D4: track 27.4 -> 30.1 mm
- net /D2: track 26.8 -> 29.3 mm
- net /D1: track 27.3 -> 29.4 mm
- net Net-(U7-CPOUT): track 1.99 -> 0.00 mm
- net /SDA2: track 17.7 -> 18.2 mm
- net +3V3: track 242.5 -> 243.0 mm
- net /SCL2: track 22.4 -> 23.0 mm

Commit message: update: I2C2 to I2C0
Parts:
- J14: value I2C2 -> I2C0
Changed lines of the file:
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@@
 			)
 		)
-		(property "Value" "I2C2"
+		(property "Value" "I2C0"
 			(at -0.175 2.9 180)
 			(layer "F.SilkS")

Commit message: fix: wrong marking TX/RX on the PCB
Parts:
- moved G*** 0.10 mm to (74.1, 88.3)
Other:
- board text added: "2.0.1"
- board text removed: "2.0.0"

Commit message: fix: wrong LED direction
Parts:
- turned D3 to 180 degrees
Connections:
- net /SCL2 renamed /SCL0
- net /SDA2 renamed /SDA0
- R8 pad 2: Net-(D3-K) -> Net-(D3-A)
- U2 pad 5: Net-(D3-A) -> Net-(D3-K)
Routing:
- net Net-(D3-K): track 1.60 -> 2.24 mm
- net Net-(D3-A): track 2.24 -> 1.60 mm

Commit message: update: remove jumpers
PCB v2.0.1
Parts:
- removed J14: I2C0, Connector_PinHeader_1.00mm:PinHeader_1x02_P1.00mm_Vertical
- removed J8: CAN, Connector_PinHeader_1.00mm:PinHeader_1x02_P1.00mm_Vertical
- removed J9: I2C1, Connector_PinHeader_1.00mm:PinHeader_1x02_P1.00mm_Vertical
- JP5: footprint Connector_PinHeader_1.00mm:PinHeader_1x02_P1.00mm_Vertical -> Connector_PinHeader_2.54mm:PinHeader_1x02_P2.54mm_Vertical
- moved JP5 1.76 mm to (116.5, 114.1), turned to 0 degrees
- moved R38 1.47 mm to (119.9, 113.6)
- moved R39 1.47 mm to (121.6, 114.3)
- turned R33 to 90 degrees
- turned R37 to 180 degrees
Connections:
- R33 pad 1: /SDA0 -> +3V3
- R33 pad 2: +3V3 -> /SDA0
- R37 pad 1: +3V3 -> /SCL0
- R37 pad 2: /SCL0 -> +3V3
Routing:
- net /SCL0: track 23.0 -> 20.3 mm, vias 1 -> 2
- net /SDA1: track 44.4 -> 42.1 mm
- net /SCL1: track 43.6 -> 41.6 mm
- net Net-(JP5-A): track 5.04 -> 3.46 mm
- net +3V3: track 243.0 -> 243.7 mm
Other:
- board text removed: "SCL"
- board text removed: "SDA"
